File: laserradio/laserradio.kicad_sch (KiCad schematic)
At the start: 83 parts, among them J1 USB4105-GF-A, J2 Conn_01x01_Female, J3 DEBUG, J4 RIGHT, SW1 SW_SPDT, SW2 SW_SPDT, U1 W25Q128JV, U2 RP2040, U3 MCP1702T-3302E_CB, U4 ADA4891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

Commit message: Fixed schematic bugs
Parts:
- C1: footprint Connector_PinHeader_2.54mm:PinHeader_1x01_P2.54mm_Vertical -> Capacitor_SMD:C_0603_1608Metric
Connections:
- net at R17.2: now also LD1.2 (K); no longer LD1.3 (K)
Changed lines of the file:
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@@
       (effects (font (size 1.27 1.27)) (justify right))
     )
-    (property "Footprint" "Connector_PinHeader_2.54mm:PinHeader_1x01_P2.54mm_Vertical" (id 2) (at 25.0952 96.52 0)
+    (property "Footprint" "Capacitor_SMD:C_0603_1608Metric" (id 2) (at 25.0952 96.52 0)
       (effects (font (size 1.27 1.27)) hide)
     )
@@
   (symbol (lib_id "Device:D_Laser_1A3C") (at 322.58 139.7 180) (unit 1)
     (in_bom yes) (on_board yes)
-    (property "Reference" "LD1" (id 0) (at 322.58 144.78 0))
-    (property "Value" "D_Laser_1A3C" (id 1) (at 322.58 147.32 0))
-    (property "Footprint" "Connector_PinHeader_2.54mm:PinHeader_1x02_P2.54mm_Vertical" (id 2) (at 325.12 139.065 0)
-      (effects (font (size 1.27 1.27)) hide)
-    )
-    (property "Datasheet" "https://media.digikey.com/pdf/Data%20Sheets/Adafruit%20PDFs/1054_Web.pdf" (id 3) (at 321.818 134.62 0)
-      (effects (font (size 1.27 1.27)) hide)
-    )
-    (pin "1")
-    (pin "3")
+    (property "Reference" "LD1" (id 0) (at 322.58 134.62 0))
+    (property "Value" "D_Laser_1A3C" (id 1) (at 322.58 132.08 0))
+    (property "Footprint" "Connector_PinHeader_2.54mm:PinHeader_1x02_P2.54mm_Vertical" (id 2) (at 321.31 147.32 0)
+      (effects (font (size 1.27 1.27)) hide)
+    )
+    (property "Datasheet" "https://media.digikey.com/pdf/Data%20Sheets/Adafruit%20PDFs/1054_Web.pdf" (id 3) (at 323.342 144.78 0)
+      (effects (font (size 1.27 1.27)) hide)
+    )
+    (pin "1")
+    (pin "2")
   )
   (symbol (lib_id "Device:Opamp_Quad") (at 310.515 55.88 0) (unit 2)
@@
     )
     (path "/2fc9b624-be90-48f2-b80c-7987b933913b"
-      (reference "C1") (unit 1) (value "0.1µF") (footprint "Connector_PinHeader_2.54mm:PinHeader_1x01_P2.54mm_Vertical")
+      (reference "C1") (unit 1) (value "0.1µF") (footprint "Capacitor_SMD:C_0603_1608Metric")
     )
     (path "/e23992fa-79b5-4597-9d36-5463246aaeb4"

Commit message: Fixed unconnected capacitor
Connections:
- net GND: now also C21.2
- net at D3.2 (A), R16.2, U6.3 (+)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: now also C21.1
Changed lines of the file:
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@@
   (junction (at 224.79 120.65) (diameter 0) (color 0 0 0 0)
   )
+  (junction (at 282.575 73.66) (diameter 0) (color 0 0 0 0)
+  )
   (junction (at 308.61 81.915) (diameter 0) (color 0 0 0 0)
   )
@@
     (stroke (width 0) (type default) (color 0 0 0 0))
   )
-  (wire (pts (xy 280.035 73.66) (xy 290.83 73.66))
+  (wire (pts (xy 280.035 73.66) (xy 282.575 73.66))
     (stroke (width 0) (type default) (color 0 0 0 0))
   )
@@
     (stroke (width 0) (type default) (color 0 0 0 0))
   )
-  (wire (pts (xy 278.13 73.66) (xy 278.13 76.2))
+  (wire (pts (xy 282.575 73.66) (xy 282.575 76.2))
+    (stroke (width 0) (type default) (color 0 0 0 0))
+  )
+  (wire (pts (xy 282.575 73.66) (xy 290.83 73.66))
     (stroke (width 0) (type default) (color 0 0 0 0))
   )
@@
     (pin "2")
   )
-  (symbol (lib_id "power:GND") (at 278.13 83.82 0) (unit 1)
+  (symbol (lib_id "power:GND") (at 282.575 83.82 0) (unit 1)
     (in_bom yes) (on_board yes)
-    (property "Reference" "#PWR037" (id 0) (at 278.13 90.17 0)
+    (property "Reference" "#PWR037" (id 0) (at 282.575 90.17 0)
       (effects (font (size 1.27 1.27)) hide)
     )
     (property "Value" "GND" (id 1) (at 282.575 88.9 0))
-    (property "Footprint" "" (id 2) (at 278.13 83.82 0)
+    (property "Footprint" "" (id 2) (at 282.575 83.82 0)
       (effects (font (size 1.27 1.27)) hide)
     )
-    (property "Datasheet" "" (id 3) (at 278.13 83.82 0)
+    (property "Datasheet" "" (id 3) (at 282.575 83.82 0)
       (effects (font (size 1.27 1.27)) hide)
     )

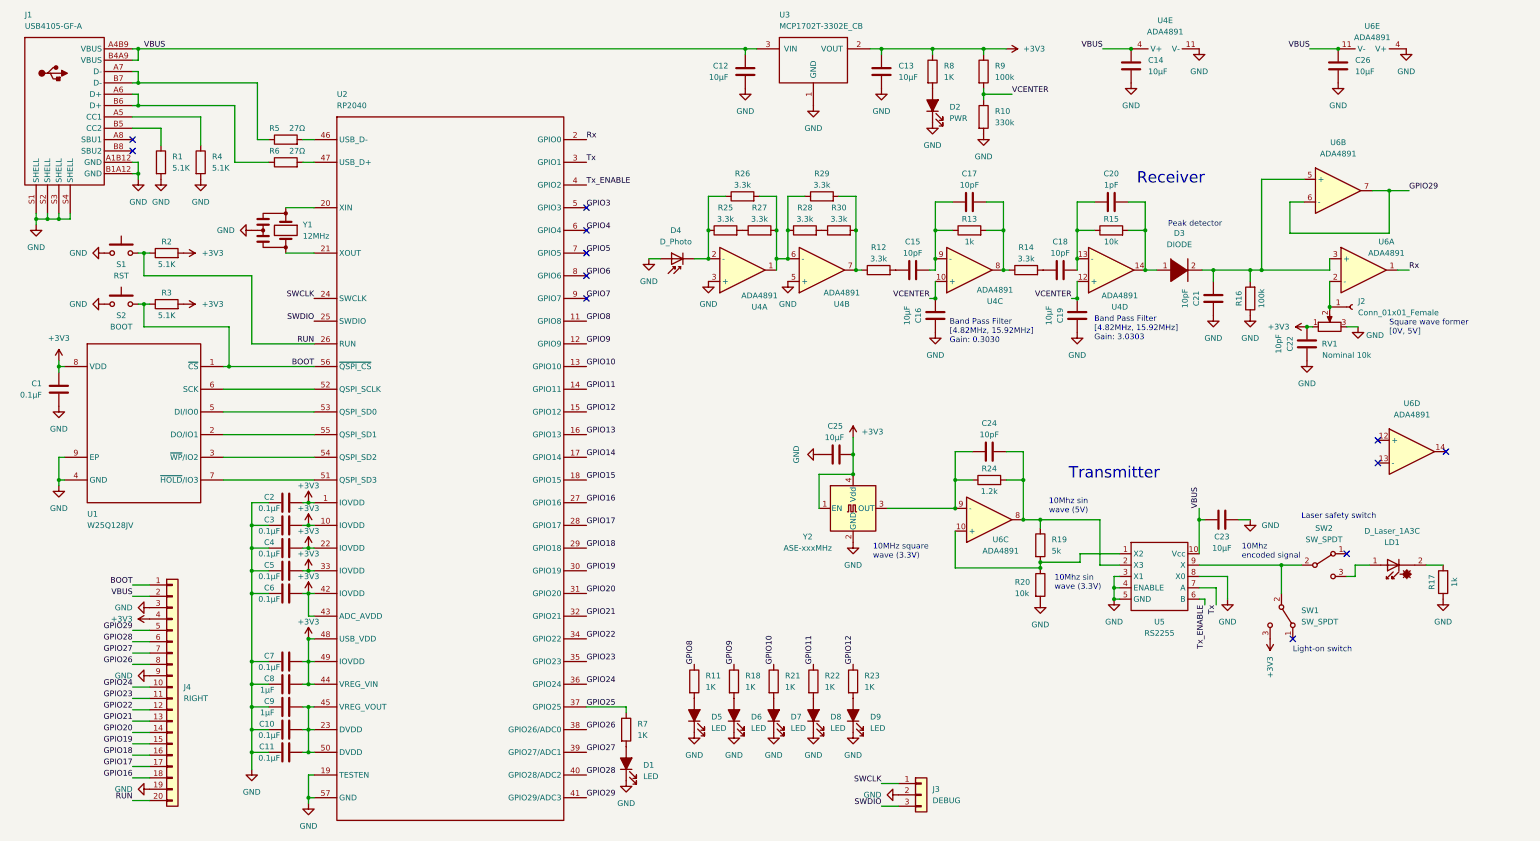
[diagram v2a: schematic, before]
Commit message: fix voltage divider (adding extra op-amp buffer) on transmit side
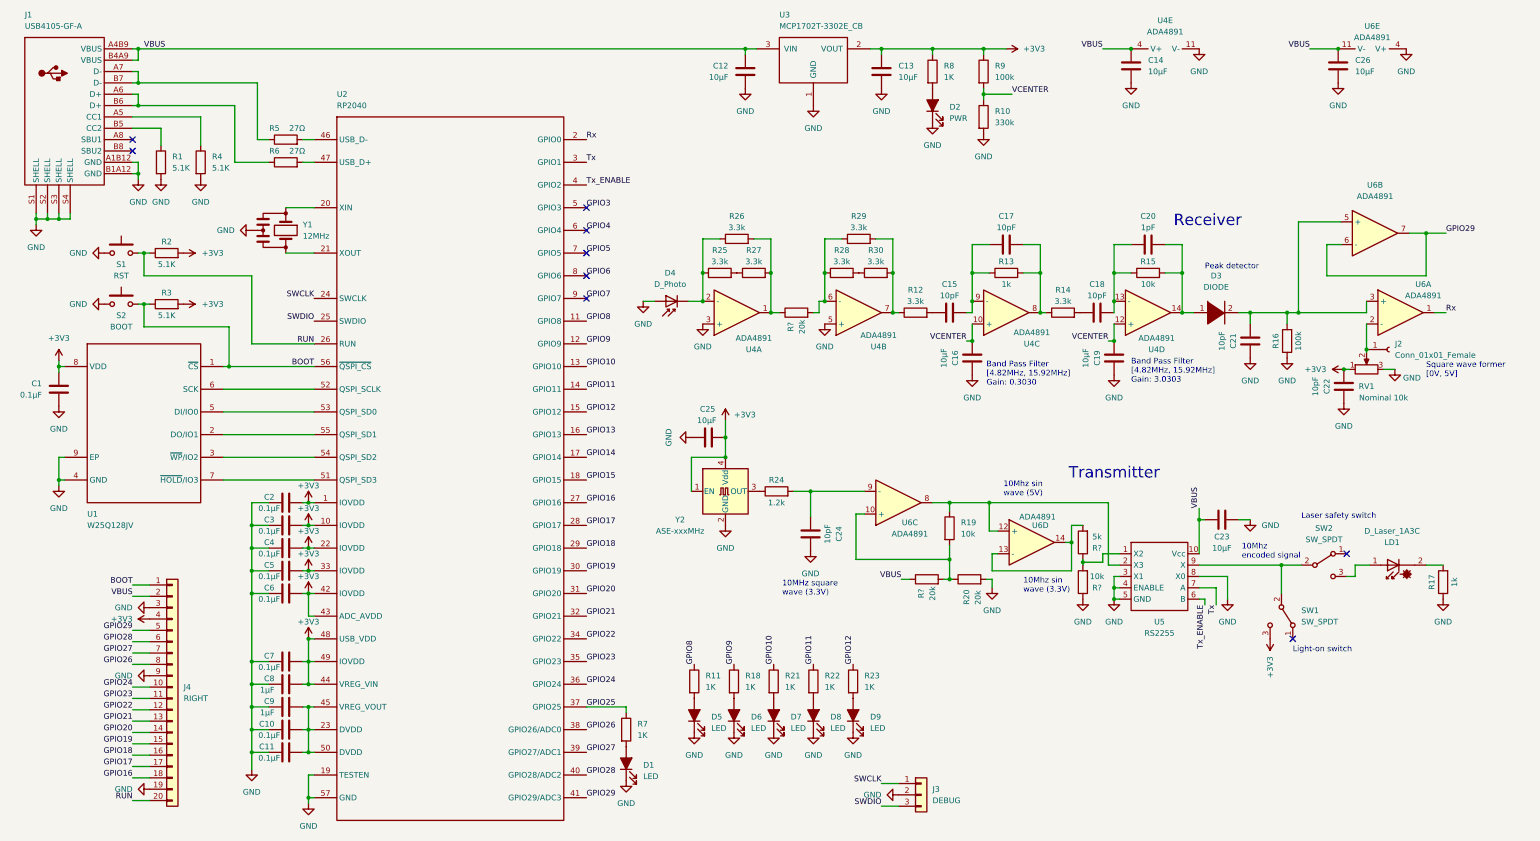
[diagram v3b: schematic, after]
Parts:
- added R? (x2): 20k, symbol Device:R
- added R?: 5k, symbol Device:R
- added R?: 10k, symbol Device:R
- R19: value 5k -> 10k
- R20: value 10k -> 20k
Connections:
- net GND: now also C24.2, R?.1
- net VBUS: now also R?.1
- net at R24.1, Y2.3 (OUT): no longer C24.1, U6.9 (-)
- net at R19.1, U5.2 (X3), U6.8: now also U6.12 (+); no longer C24.2, R24.2
- net at U6.13 (-): now also U6.14, R?.2
- net at R28.1, R29.1, U4.6 (-): now also R?.2; no longer R26.2, R27.2, U4.1
- net at R19.2, R20.1, U6.10 (+): now also R?.2; no longer U5.1 (X2)
- new net: C24.1, R24.2, U6.9 (-)
- new net: R26.2, R27.2, R?.1, U4.1
- new net: R?.1, R?.2, U5.1 (X2)
- no-connect marks 12 -> 9
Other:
- moved on the sheet: C15, C16, C17, C18, C19, C20, C21, C22, C24, C25, D3, D4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

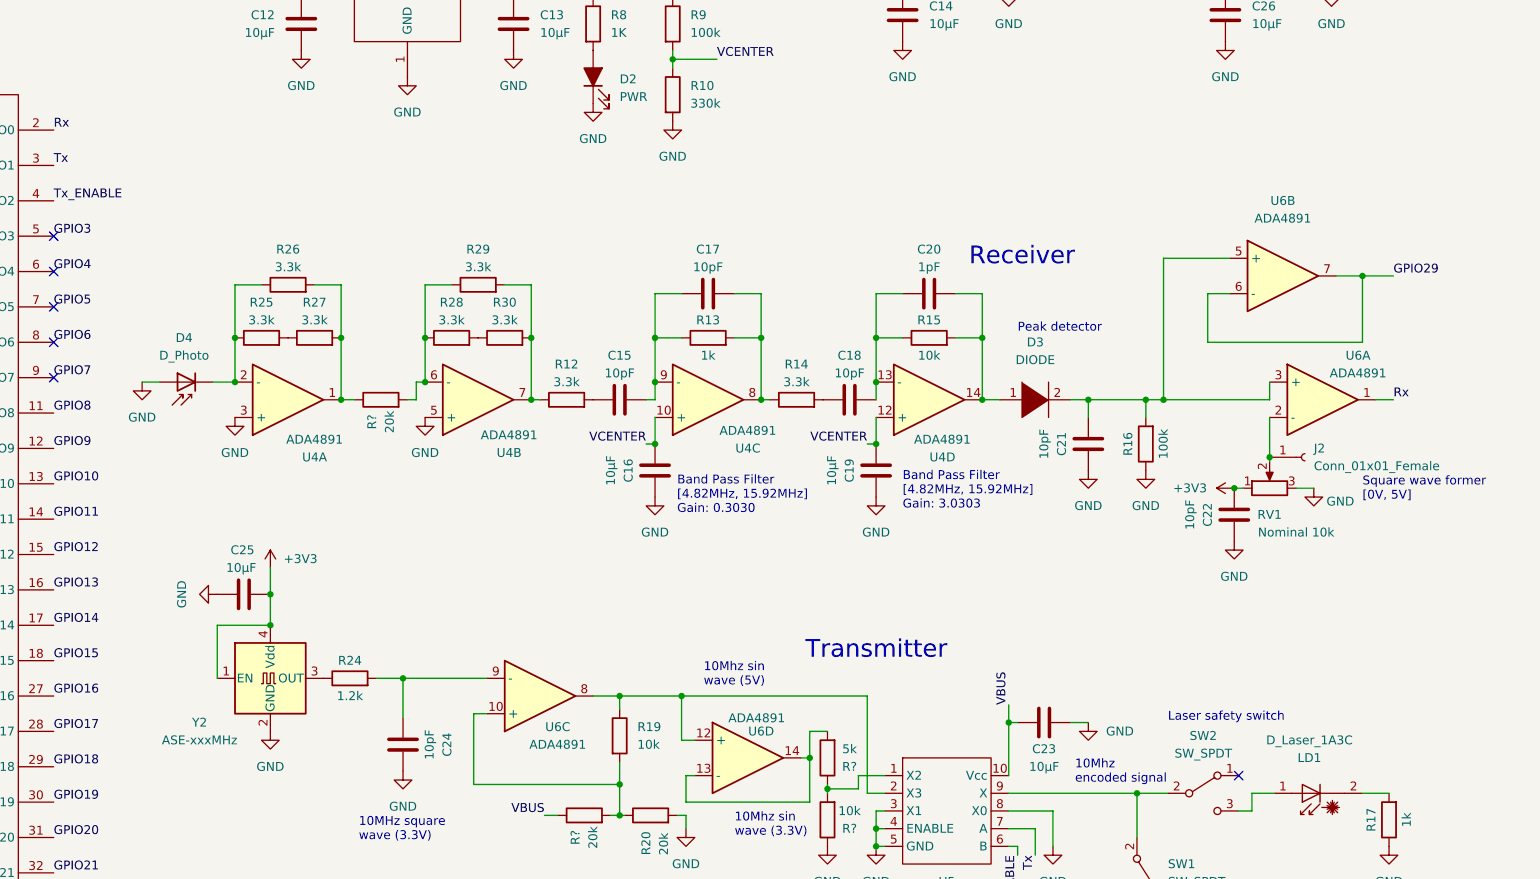
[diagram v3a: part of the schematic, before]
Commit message: configure second amplifier to have variable gain
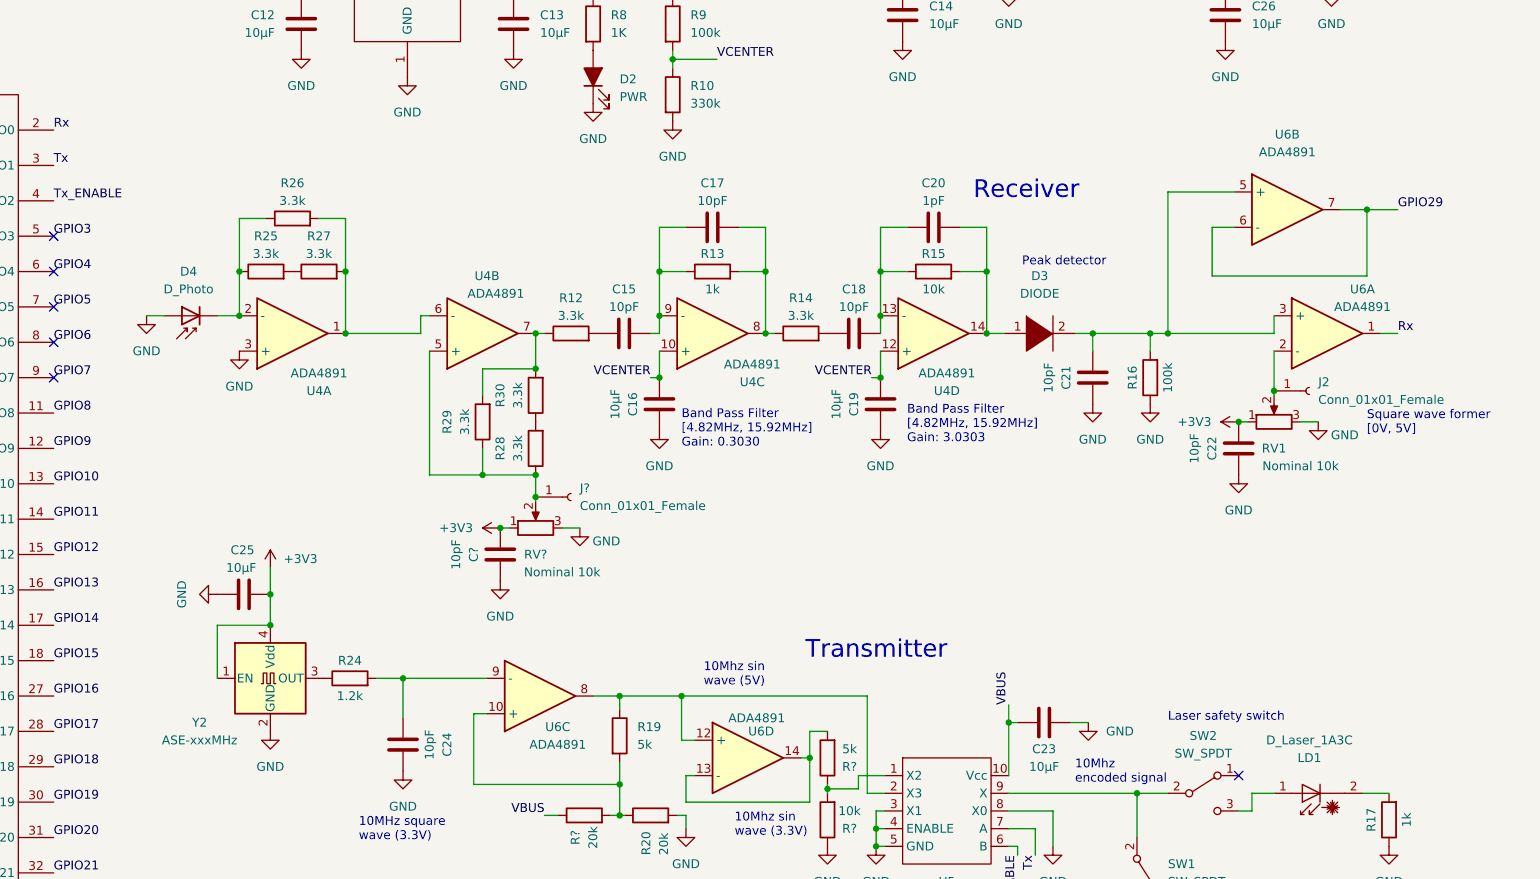
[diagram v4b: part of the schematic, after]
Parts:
- removed R?: 20k, symbol Device:R
- added C?: 10pF, Capacitor_SMD:C_0603_1608Metric, symbol Device:C
- added J?: Conn_01x01_Female, Connector_PinHeader_2.54mm:PinHeader_1x01_P2.54mm_Vertical, symbol Connector:Conn_01x01_Female
- added RV?: Nominal 10k, Eclectronics:Laser Potentiometer, symbol Device:R_Potentiometer
- R19: value 10k -> 5k
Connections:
- net +3V3: now also C?.1, RV?.1
- net GND: now also C?.2, RV?.3; no longer U4.5 (+)
- net at R28.1, R29.1: now also U4.5 (+), J?.1 (Pin_1), RV?.2; no longer U4.6 (-)
- net at R26.2, R27.2, U4.1: now also U4.6 (-)
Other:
- moved on the sheet: C15, C16, C17, C18, C19, C20, C21, C22, D3, D4, J2, R12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
